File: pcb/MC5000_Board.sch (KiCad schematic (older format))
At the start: 0 parts

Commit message: One PCB to rule them all
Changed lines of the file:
@@
 $Descr A4 11693 8268
 encoding utf-8
-Sheet 1 11
+Sheet 1 15
 Title ""
 Date ""
@@
 F0 "USB serial" 50
 F1 "modules/USB_serial.sch" 50
+$EndSheet
+$Sheet
+S 750  750  1600 1100
+U 60303416
+F0 "PFS172 breakout - MCU1" 50
+F1 "modules/PFS172_breakout.sch" 50
+$EndSheet
+$Sheet
+S 2650 800  1600 1050
+U 6030344A
+F0 "PFS172 breakout - MCU2" 50
+F1 "modules/PFS172_breakout.sch" 50
 $EndSheet
 $Sheet
@@
 $EndSheet
 $Sheet
-S 900  850  1600 1050
+S 5000 3700 1600 1050
 U 603839E8
 F0 "Connection block" 50
 F1 "connection_block.sch" 50
 $EndSheet
+$Sheet
+S 2650 2200 1600 1050
+U 602FB936
+F0 "PFS172 breakout - Display Ctrl" 50
+F1 "modules/PFS172_breakout.sch" 50
+$EndSheet
+$Sheet
+S 750  2200 1600 1050
+U 603034BC
+F0 "PFS172 breakout - Buzzer" 50
+F1 "modules/PFS172_breakout.sch" 50
+$EndSheet
 $EndSCHEMATC

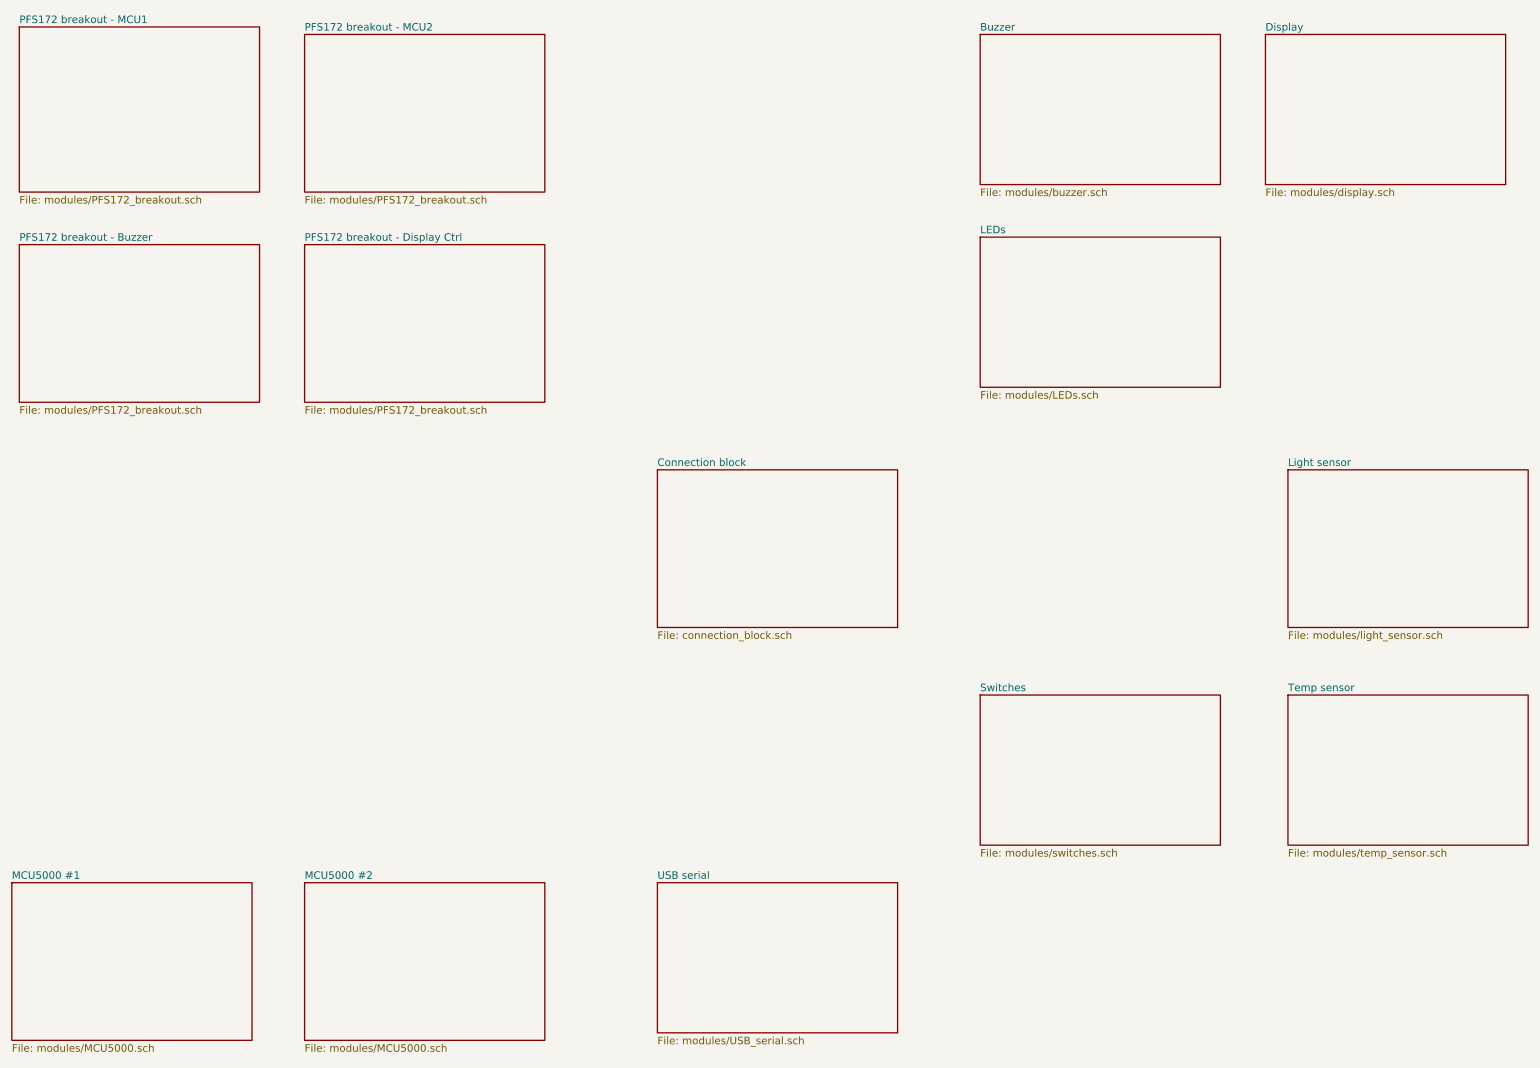
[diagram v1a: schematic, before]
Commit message: Changed overview schematic
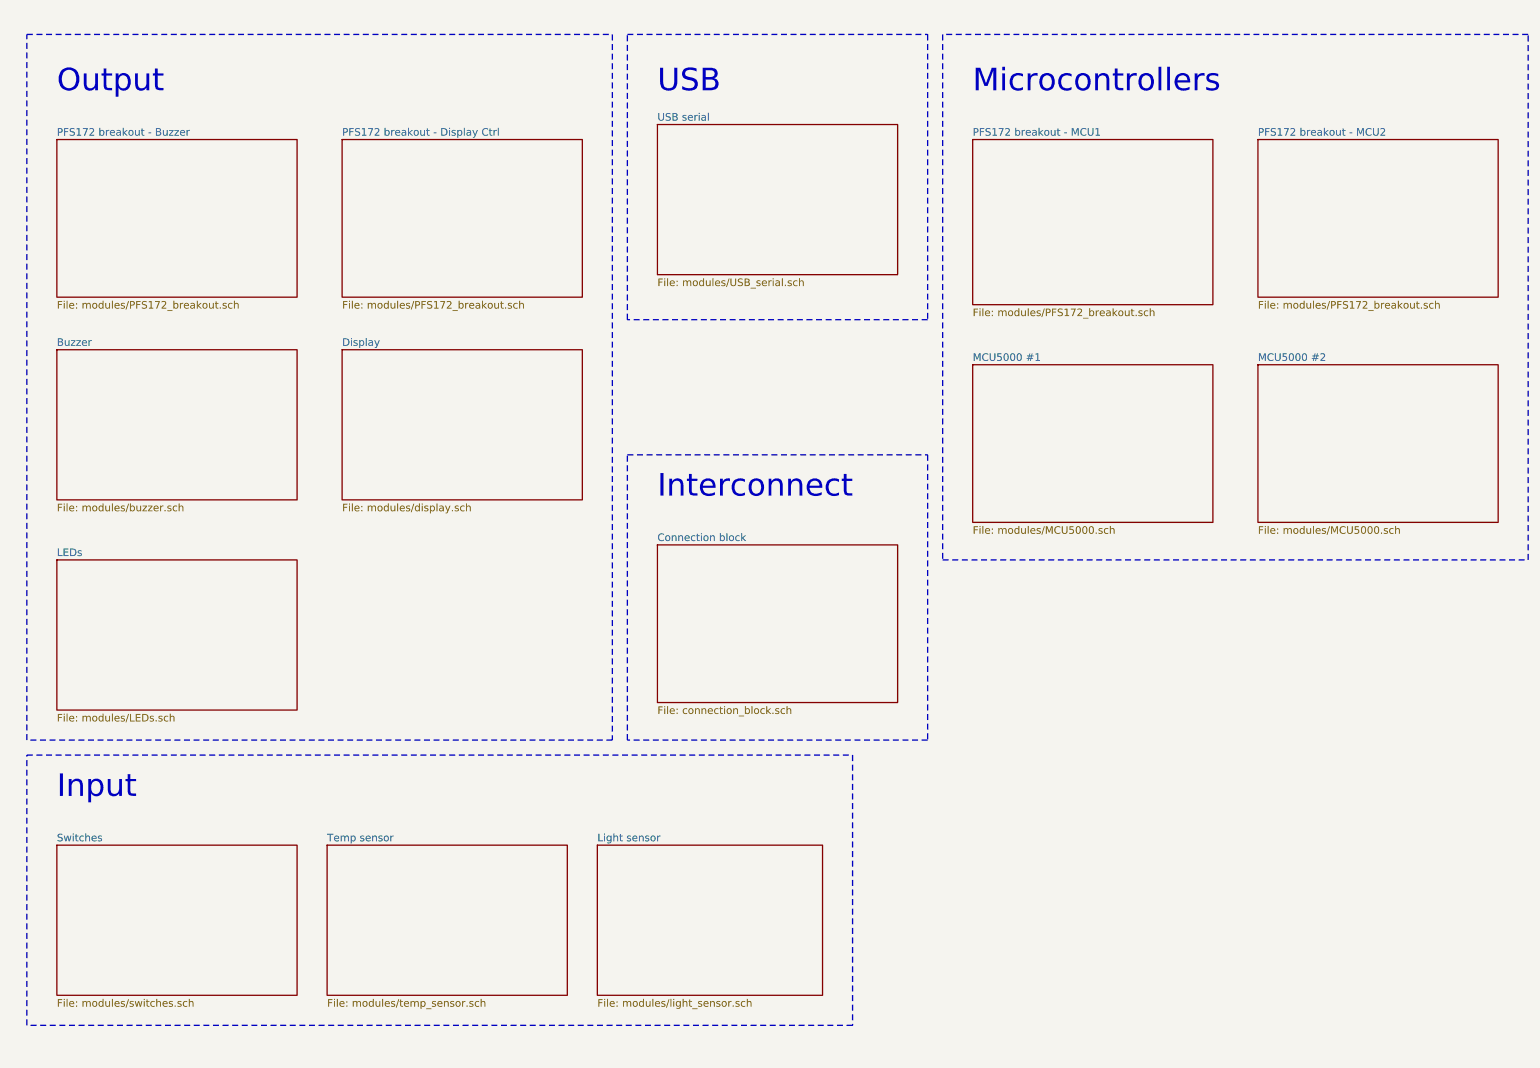
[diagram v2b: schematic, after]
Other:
- note added: "Input"
- note added: "Interconnect"
- note added: "Microcontrollers"
- note added: "Output"
- note added: "USB"
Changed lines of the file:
@@
 $EndDescr
 $Sheet
-S 5000 6450 1600 1000
+S 5000 1400 1600 1000
 U 602FF29A
 F0 "USB serial" 50
@@
 $EndSheet
 $Sheet
-S 750  750  1600 1100
+S 7100 1500 1600 1100
 U 60303416
 F0 "PFS172 breakout - MCU1" 50
@@
 $EndSheet
 $Sheet
-S 2650 800  1600 1050
+S 9000 1500 1600 1050
 U 6030344A
 F0 "PFS172 breakout - MCU2" 50
@@
 $EndSheet
 $Sheet
-S 9050 800  1600 1000
+S 2900 2900 1600 1000
 U 60308700
 F0 "Display" 50
@@
 $EndSheet
 $Sheet
-S 700  6450 1600 1050
+S 7100 3000 1600 1050
 U 6034DF24
 F0 "MCU5000 #1" 50
@@
 $EndSheet
 $Sheet
-S 2650 6450 1600 1050
+S 9000 3000 1600 1050
 U 603599D1
 F0 "MCU5000 #2" 50
@@
 $EndSheet
 $Sheet
-S 7150 800  1600 1000
+S 1000 2900 1600 1000
 U 603632C9
 F0 "Buzzer" 50
@@
 $EndSheet
 $Sheet
-S 7150 2150 1600 1000
+S 1000 4300 1600 1000
 U 6036720E
 F0 "LEDs" 50
@@
 $EndSheet
 $Sheet
-S 7150 5200 1600 1000
+S 1000 6200 1600 1000
 U 6037B4F8
 F0 "Switches" 50
@@
 $EndSheet
 $Sheet
-S 9200 5200 1600 1000
+S 2800 6200 1600 1000
 U 6038A837
 F0 "Temp sensor" 50
@@
 $EndSheet
 $Sheet
-S 9200 3700 1600 1050
+S 4600 6200 1500 1000
 U 6038ECB3
 F0 "Light sensor" 50
@@
 $EndSheet
 $Sheet
-S 5000 3700 1600 1050
+S 5000 4200 1600 1050
 U 603839E8
 F0 "Connection block" 50
@@
 $EndSheet
 $Sheet
-S 2650 2200 1600 1050
+S 2900 1500 1600 1050
 U 602FB936
 F0 "PFS172 breakout - Display Ctrl" 50
@@
 $EndSheet
 $Sheet
-S 750  2200 1600 1050
+S 1000 1500 1600 1050
 U 603034BC
 F0 "PFS172 breakout - Buzzer" 50
 F1 "modules/PFS172_breakout.sch" 50
 $EndSheet
+Text Notes 7100 1200 0    150  ~ 0
+Microcontrollers
+Wire Notes Line
+	6900 800  6900 4300
+Wire Notes Line
+	6900 4300 10800 4300
+Wire Notes Line
+	10800 4300 10800 800
+Wire Notes Line
+	10800 800  6900 800
+Text Notes 5000 3900 0    150  ~ 0
+Interconnect
+Wire Notes Line
+	4800 3600 6800 3600
+Wire Notes Line
+	6800 3600 6800 5500
+Wire Notes Line
+	6800 5500 4800 5500
+Wire Notes Line
+	4800 5500 4800 3600
+Text Notes 5000 1200 0    150  ~ 0
+USB
+Wire Notes Line
+	4800 800  6800 800
+Wire Notes Line
+	6800 800  6800 2700
+Wire Notes Line
+	6800 2700 4800 2700
+Wire Notes Line
+	4800 2700 4800 800
+Text Notes 1000 1200 0    150  ~ 0
+Output
+Wire Notes Line
+	800  800  4700 800
+Wire Notes Line
+	4700 800  4700 5500
+Wire Notes Line
+	4700 5500 800  5500
+Wire Notes Line
+	800  5500 800  800
+Text Notes 1000 5900 0    150  ~ 0
+Input
+Wire Notes Line
+	800  5600 6300 5600
+Wire Notes Line
+	6300 5600 6300 7400
+Wire Notes Line
+	6300 7400 800  7400
+Wire Notes Line
+	800  7400 800  5600
 $EndSCHEMATC
